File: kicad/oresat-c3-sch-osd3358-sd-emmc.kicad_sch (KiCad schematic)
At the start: 42 parts, among them J5 DM3BT-DSF-PEJS, U1 OSD3358-512M-BSM, U8 TCAN330, U9 EMMC+RESET+5.1-COMPATIBLE-BA

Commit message: Zero airwires! Rough draft schematic and layout are done. Still need ERC and DRC and full design review and stiching and polish.
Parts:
- removed TP31: Test-Point, oresat-misc:TestPoint_Pad_D1.0mm, symbol oresat-misc:Test-Point-1mm-round
- added TP25, TP86, TP87: Test-Point, oresat-misc:TestPoint_Pad_D1.0mm, symbol oresat-misc:Test-Point-1mm-round
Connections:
- net LBAND_LO_SCLK is gone; now on net FIRE_HELICAL_1: U1.B2 (MCASP0_AXR0)
- net LBAND_LO_SDATA is gone; now on net TEST_ANTENNAS: U1.B1 (MCASP0_AHCLKR)
- net LBAND_LO_nSEN is gone; now on net TEST_HELICAL: U1.A2 (MCASP0_FSX)
- net RADIO-nFLT is gone; now on an unnamed net: U1.T5 (GPMC_AD11)
- net FIRE_ANTENNAS_1: now also U1.B4 (XDMA_EVENT_INTR1); no longer U1.N2 (GPMC_WEN)
- net FIRE_ANTENNAS_2: now also U1.C4 (MCASP0_AHCLKX); no longer U1.N1 (GPMC_OEN_REN)
- net FIRE_HELICAL_1: no longer U1.M1 (GPMC_ADVN_ALE)
- net FIRE_HELICAL_2: now also U1.A1 (MCASP0_ACLKX); no longer U1.N3 (GPMC_BEN0_CLE)
- net LBAND_IRQ: now also U1.T16 (GPMC_A11); no longer U1.A1 (MCASP0_ACLKX)
- net OPD_nENABLE: now also U1.C3 (MCASP0_AXR1); no longer U1.B4 (XDMA_EVENT_INTR1)
- net OPD_nFAULT: now also U1.B3 (MCASP0_FSR); no longer U1.C4 (MCASP0_AHCLKX)
- net TEST_ANTENNAS: no longer U1.P6 (GPMC_AD12)
- net TEST_HELICAL: no longer U1.R6 (GPMC_AD13)
- net UHF_PA_ENABLE: now also U1.P15 (GPMC_WAIT0); no longer U1.T16 (GPMC_A11)
- net UHF_TOT_CLEAR: now also U1.R16 (GPMC_WPN); no longer U1.P15 (GPMC_WAIT0)
- net UHF_TOT_OK: now also U1.R15 (GPMC_A10); no longer U1.N14 (GPMC_BEN1)
- net at TP46.1: now also U1.R6 (GPMC_AD13); no longer U1.R16 (GPMC_WPN)
- net CAN_TXD: now reaches U1.A11 (UART1_RXD), U8.1 (TXD)
- net CAN_RXD: now reaches U1.B11 (UART1_TXD), U8.4 (RXD)
- net MMC0_DAT1: now reaches J5.8 (DAT1), R69.4 (44), U1.A15 (MMC0_DAT1)
- net MMC0_DAT0: now reaches J5.7 (DAT0/DO), U1.A16 (MMC0_DAT0)
- net MMC0_DAT0: now also R69.9 (99); no longer R69.7 (77)
- net MMC0_CLK: now reaches J5.5 (CLK), R69.3 (33), U1.B15 (MMC0_CLK)
- net MMC0_CMD: now reaches J5.3 (CMD/DI), R69.8 (88), U1.B16 (MMC0_CMD)
- net MMC0_CD: now reaches J5.CD (CD#), R69.6 (66), U1.C14 (SPI0_CS1)
- net MMC0_DAT3: now reaches J5.2 (DAT3/CS), R69.2 (22), U1.C15 (MMC0_DAT3)
- net MMC0_DAT2: now reaches J5.1 (DAT2), U1.C16 (MMC0_DAT2)
- net MMC0_DAT2: now also R69.7 (77); no longer R69.9 (99)
- net at TP32.1: no longer U1.C3 (MCASP0_AXR1)
- net at TP42.1: now also U1.P6 (GPMC_AD12); no longer U1.R15 (GPMC_A10)
- net LBAND_LO_nLOCKED renamed RADIO_nFLT
- net RADIO-ENABLE: no longer names the net of U1.R5 (GPMC_AD10)
- new net: TP87.1, U1.N1 (GPMC_OEN_REN)
- new net: TP86.1, U1.N2 (GPMC_WEN)
- new net: TP25.1, U1.N3 (GPMC_BEN0_CLE)
- no-connect marks 8 -> 11
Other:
- moved on the sheet: TP32, TP42, TP46

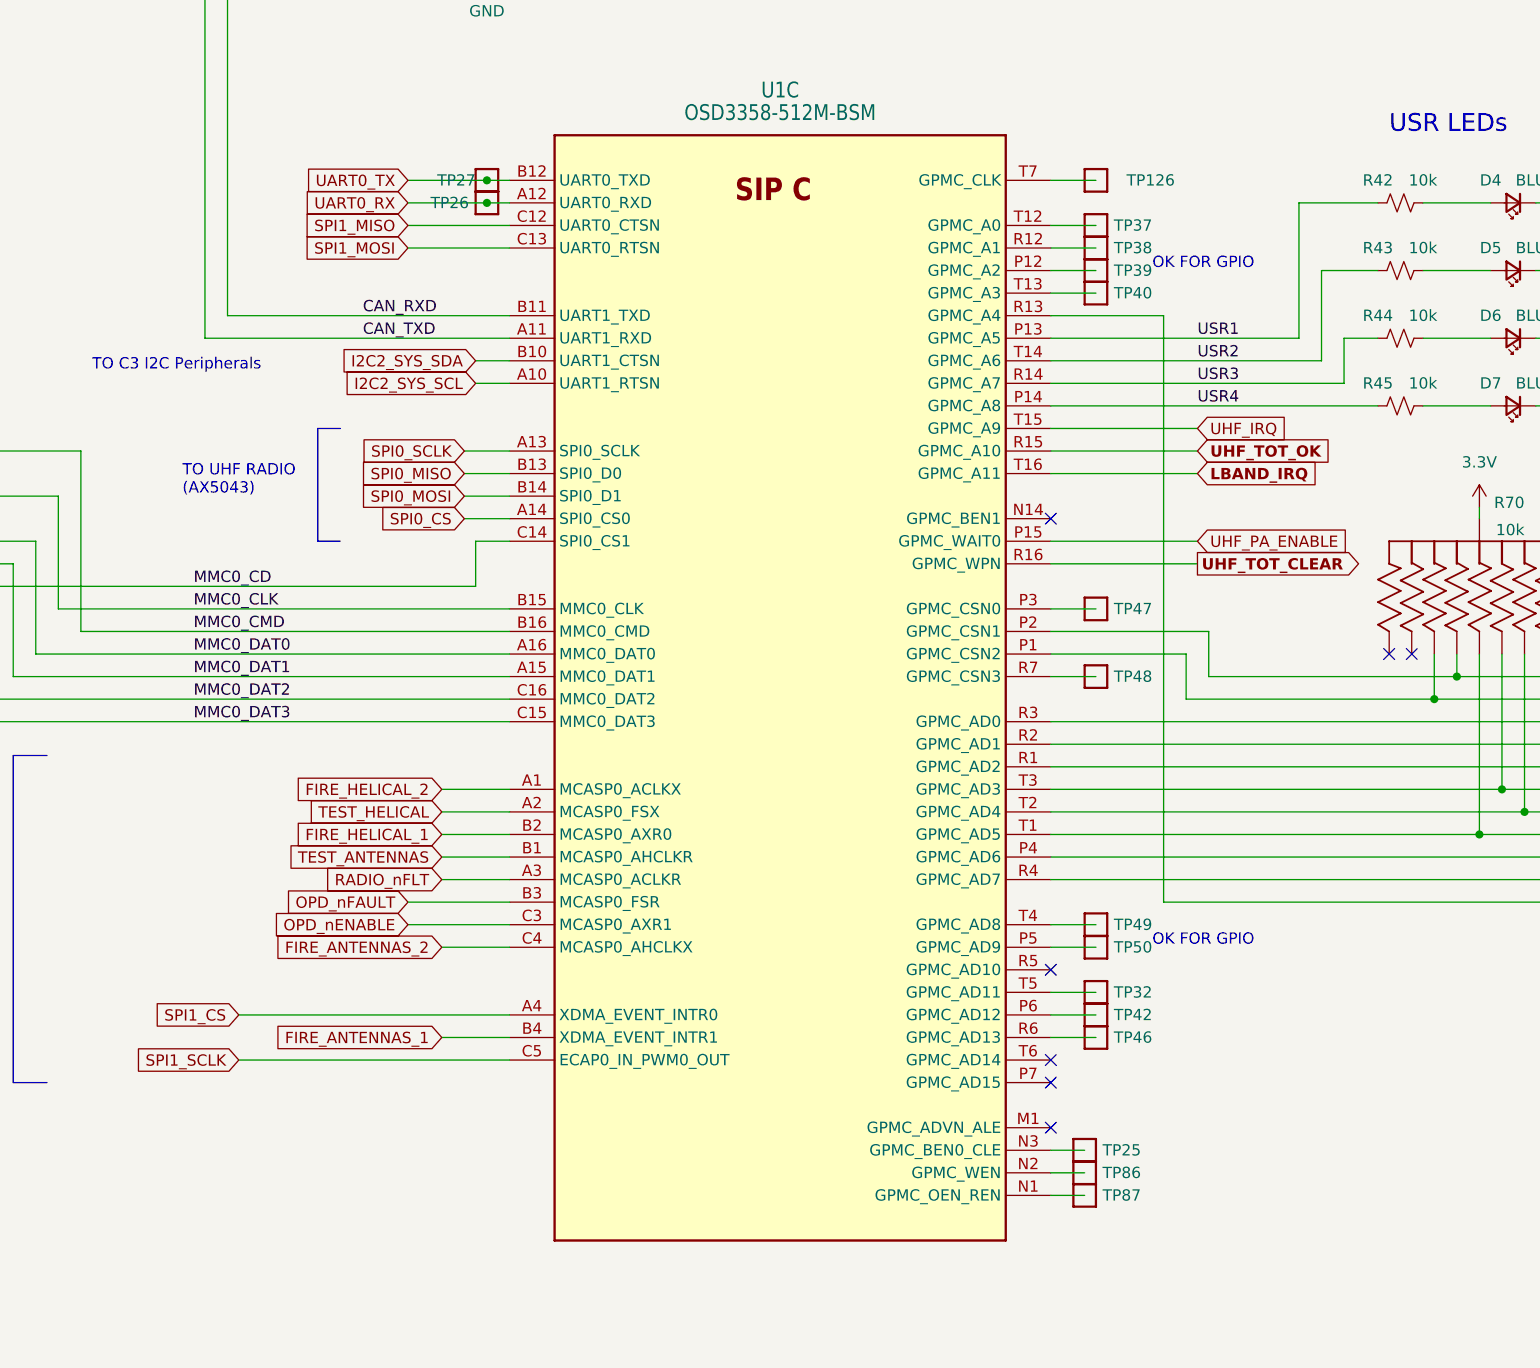
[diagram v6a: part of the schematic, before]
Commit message: Added reset states of GPIO lines to OSD3358 pins in schematic so we know what pulls up unexpectedly. Re-arranged a few pins that should not pull up on boot.
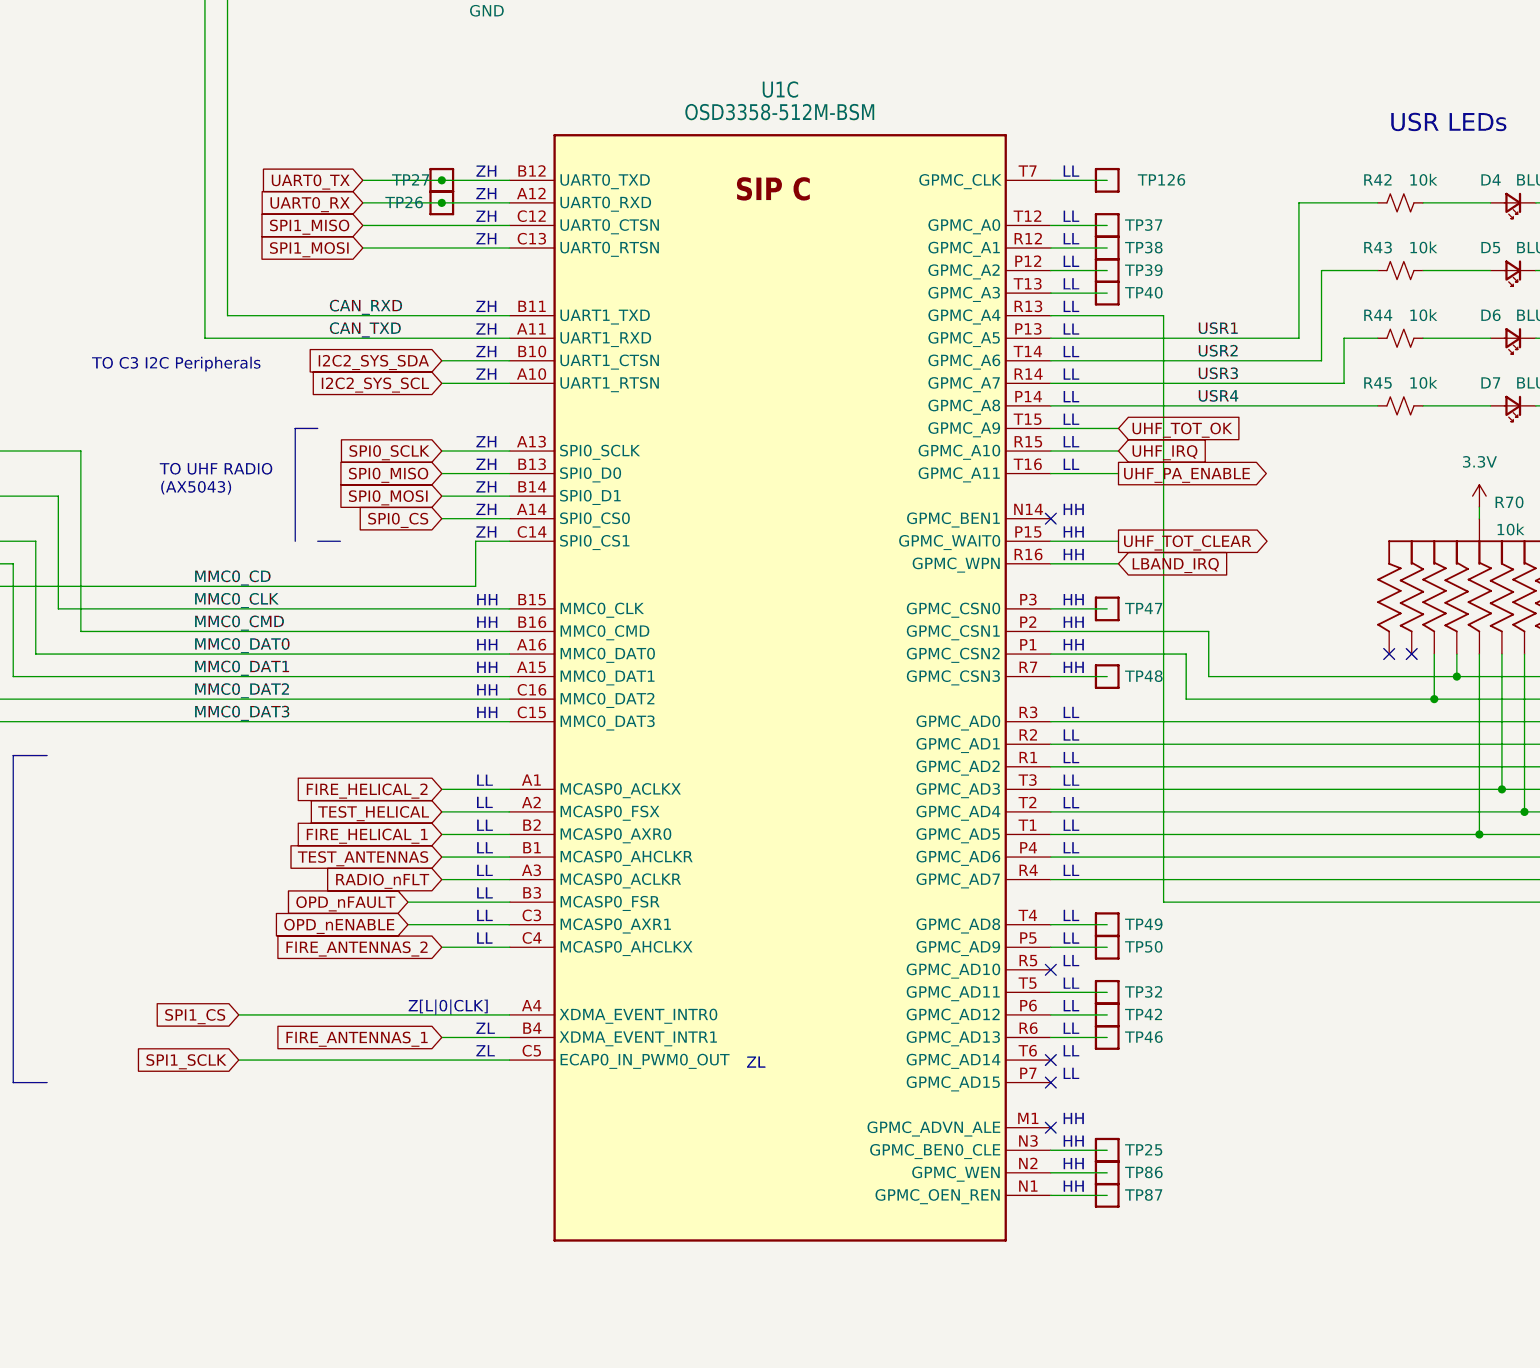
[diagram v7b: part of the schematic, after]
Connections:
- net LBAND_IRQ: now also U1.R16 (GPMC_WPN); no longer U1.T16 (GPMC_A11)
- net UHF_IRQ: now also U1.R15 (GPMC_A10); no longer U1.T15 (GPMC_A9)
- net UHF_PA_ENABLE: now also U1.T16 (GPMC_A11); no longer U1.P15 (GPMC_WAIT0)
- net UHF_TOT_CLEAR: now also U1.P15 (GPMC_WAIT0); no longer U1.R16 (GPMC_WPN)
- net UHF_TOT_OK: now also U1.T15 (GPMC_A9); no longer U1.R15 (GPMC_A10)
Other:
- note added: "HH"
- note added: "LL"
- note added: "ZH"
- note added: "ZL"
- note added: "Z[L|0|CLK]"
- note removed: "OK FOR GPIO"
- moved on the sheet: TP126, TP25, TP26, TP27, TP32, TP37, TP38, TP39, TP40, TP42, TP46, TP47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

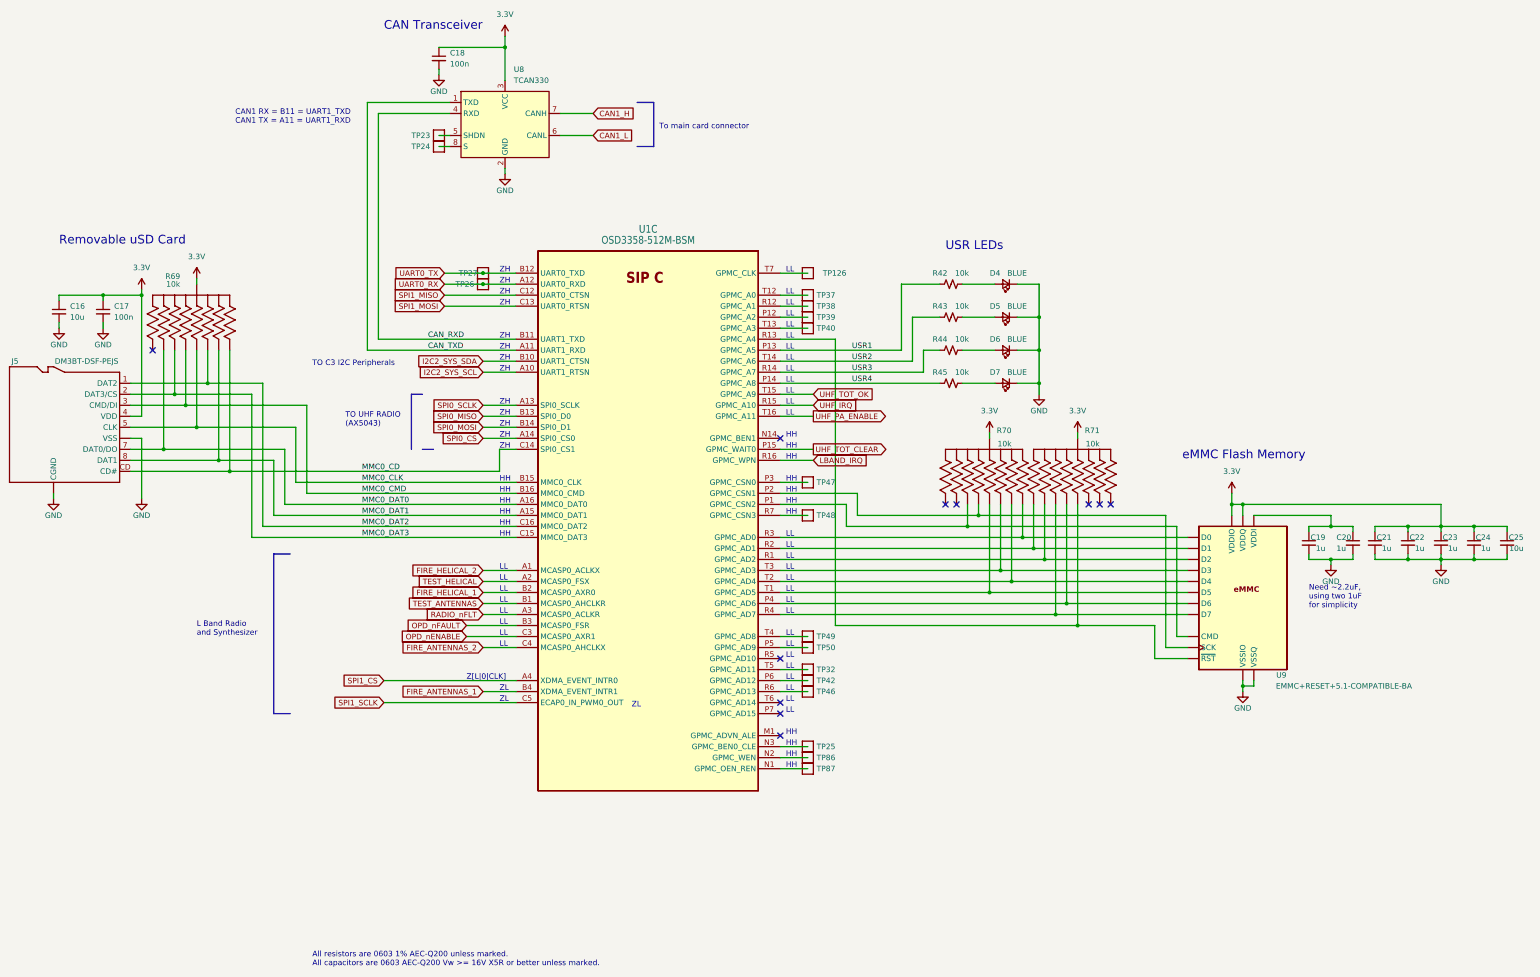
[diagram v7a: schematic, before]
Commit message: An evening of cleanups from the design review. Includes lots of ERC and DRC cleanup, although still over 450 DRC errors mostly from RF keepouts. Fixed PA ground connection, notes on pin reset configuration, and lots of small naggy things. Also cleaned up wierd broken traces on eMMC traces. No longer all same length (sorry Oliver) but it shouldn't affect performance.
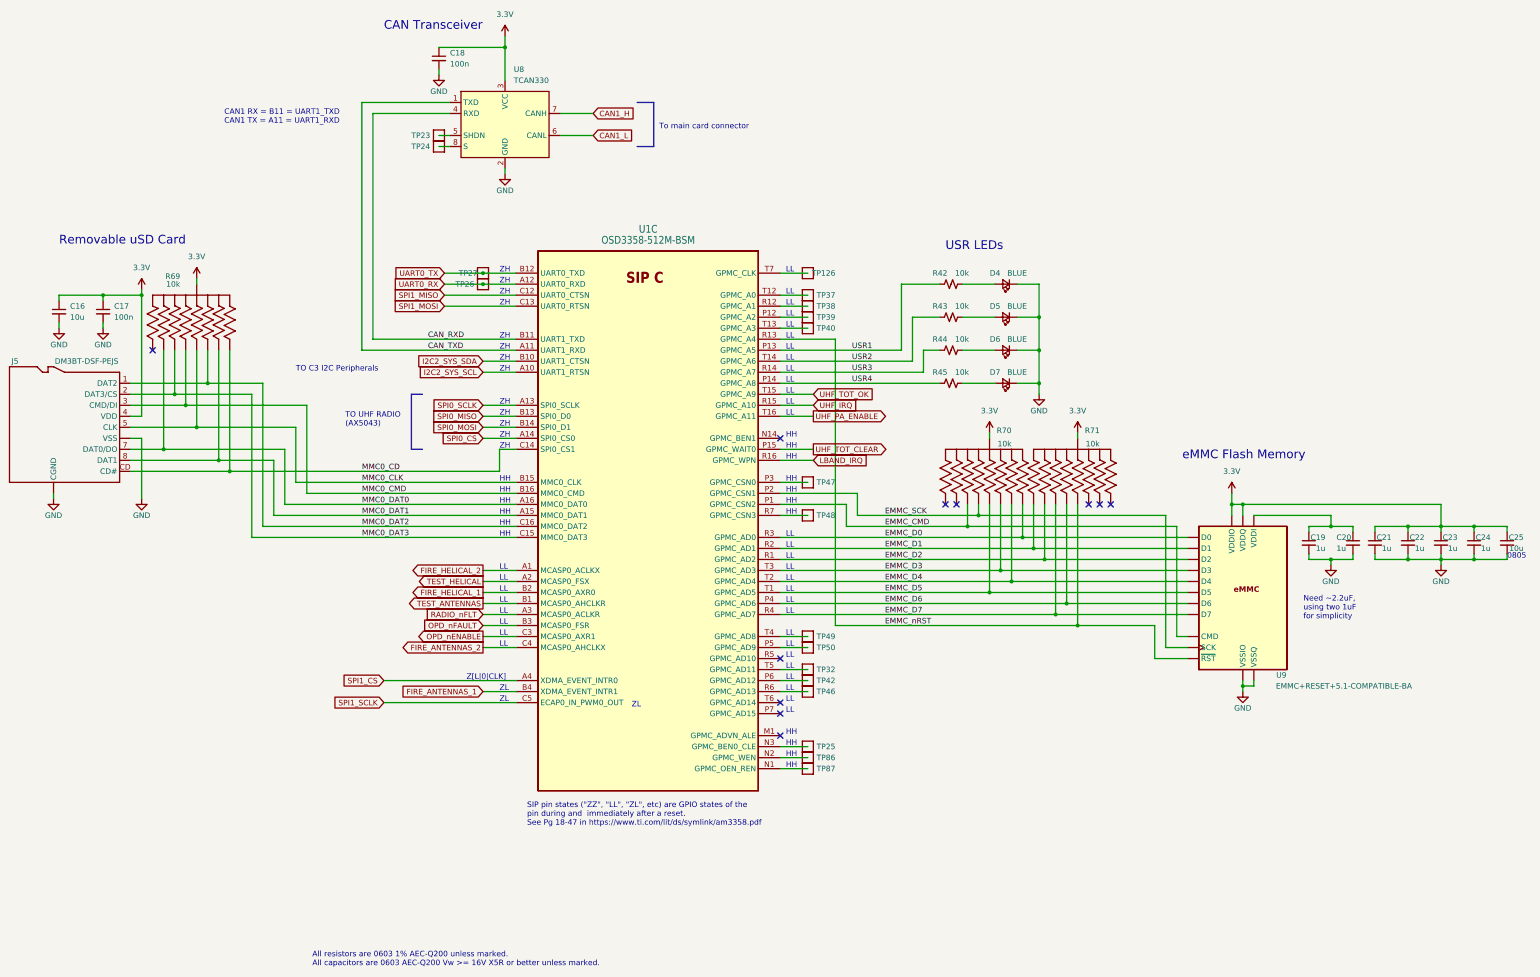
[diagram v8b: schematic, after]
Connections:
- net GND: now also U9.A2 (NC), U9.B7 (NC)
- net EMMC_D0: now reaches R70.6 (66), U1.R3 (GPMC_AD0), U9.A3 (D0)
- net EMMC_D1: now reaches R71.1 (11), U1.R2 (GPMC_AD1), U9.A4 (D1)
- net EMMC_D2: now reaches R71.9 (99), U1.R1 (GPMC_AD2), U9.A5 (D2)
- net EMMC_D3: now reaches R70.7 (77), U1.T3 (GPMC_AD3), U9.B2 (D3)
- net EMMC_D4: now reaches R70.4 (44), U1.T2 (GPMC_AD4), U9.B3 (D4)
- net EMMC_D5: now reaches R70.3 (33), U1.T1 (GPMC_AD5), U9.B4 (D5)
- net EMMC_D6: now reaches R71.8 (88), U1.P4 (GPMC_AD6), U9.B5 (D6)
- net EMMC_D7: now reaches R71.2 (22), U1.R4 (GPMC_AD7), U9.B6 (D7)
- net EMMC_nRST: now reaches R71.3 (33), U1.R13 (GPMC_A4), U9.K5 (~{RST})
- net EMMC_CMD: now reaches R70.2 (22), U1.P1 (GPMC_CSN2), U9.M5 (CMD)
- net EMMC_SCK: now reaches R70.8 (88), U1.P2 (GPMC_CSN1), U9.M6 (SCK)
- now unconnected: U9.A1 (NC), U9.A10 (NC), U9.A11 (NC), U9.A12 (NC), U9.A13 (NC), U9.A14 (NC), U9.A7 (NC), U9.A8 (NC), U9.A9 (NC)
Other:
- note added: "0805"
- note added: "SIP pin states ("ZZ", "LL", "ZL", etc) are GPIO states of the pin during and immediately after a reset. See Pg 18-47 in https://www.ti.com/lit/ds/symlink/am3358.pdf"
- note removed: "L Band Radio and Synthesizer"
